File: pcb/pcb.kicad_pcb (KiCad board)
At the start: 2 copper layers, 266.7 x 76.2 mm, 116 parts, among them J1 USB_C_Receptacle_USB2.0, SW1 SW_Push, SW10 SW_Push, SW11 SW_Push, SW12 SW_Push, SW13 SW_Push, SW14 SW_Push, SW15 SW_Push, SW16 SW_Push, SW17 SW_Push, SW18 SW_Push, SW19 SW_Push, SW2 SW_Push, SW20 SW_Push, SW21 SW_Push, SW22 SW_Push, SW23 SW_Push, SW24 SW_Push, SW25 SW_Push, SW26 SW_Push, SW27 SW_Push, SW28 SW_Push, SW29 SW_Push, SW3 SW_Push, SW30 SW_Push, SW31 SW_Push, SW32 SW_Push, SW33 SW_Push, SW34 SW_Push, SW35 SW_Push, SW36 SW_Push, SW37 SW_Push, SW38 SW_Push, SW39 SW_Push, SW4 SW_Push, SW40 SW_Push, SW41 SW_Push, SW42 SW_Push, SW43 SW_Push, SW44 SW_Push, SW45 SW_Push, SW46 SW_Push, SW47 SW_Push, SW48 SW_Push, SW49 SW_Push, SW5 SW_Push, SW6 SW_Push, SW7 SW_Push, SW8 SW_Push, SW9 SW_Push, U1 ATmega32U4-AU, Y1 16MHz

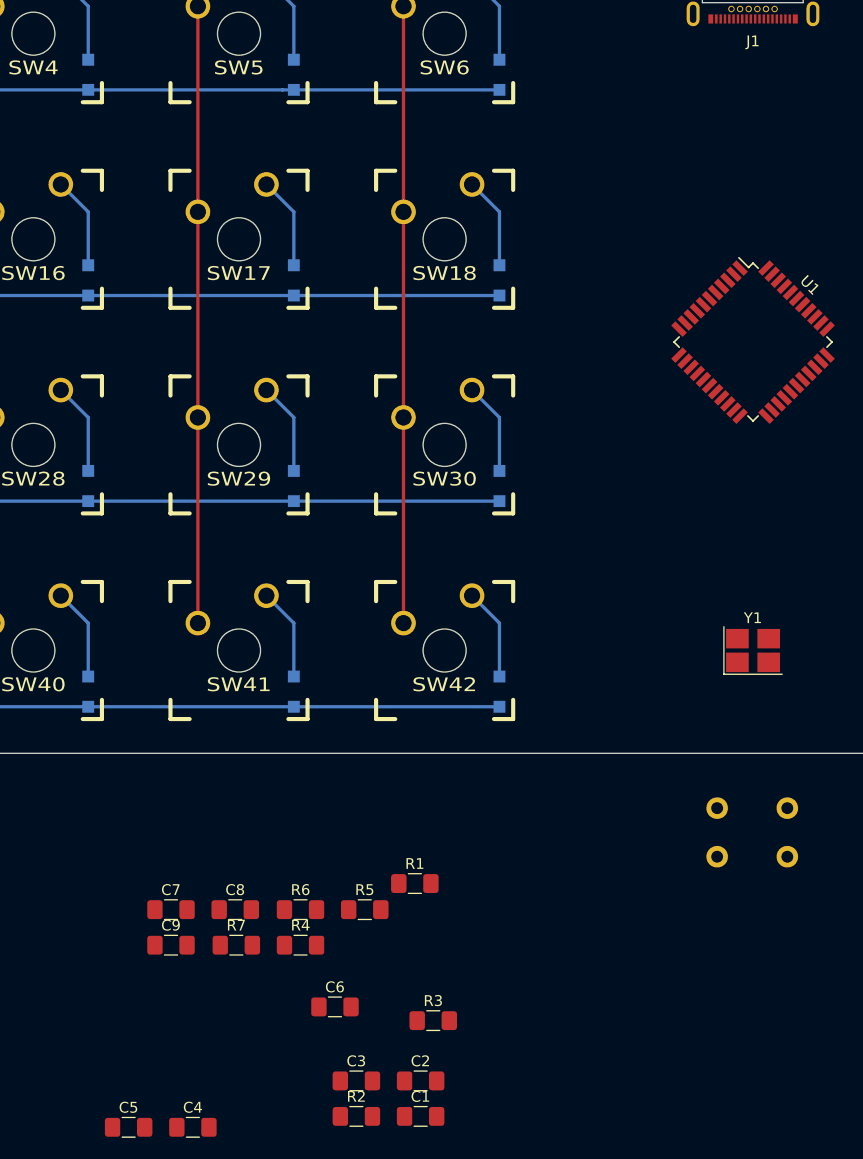
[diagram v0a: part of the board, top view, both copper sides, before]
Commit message: update USB-C pins
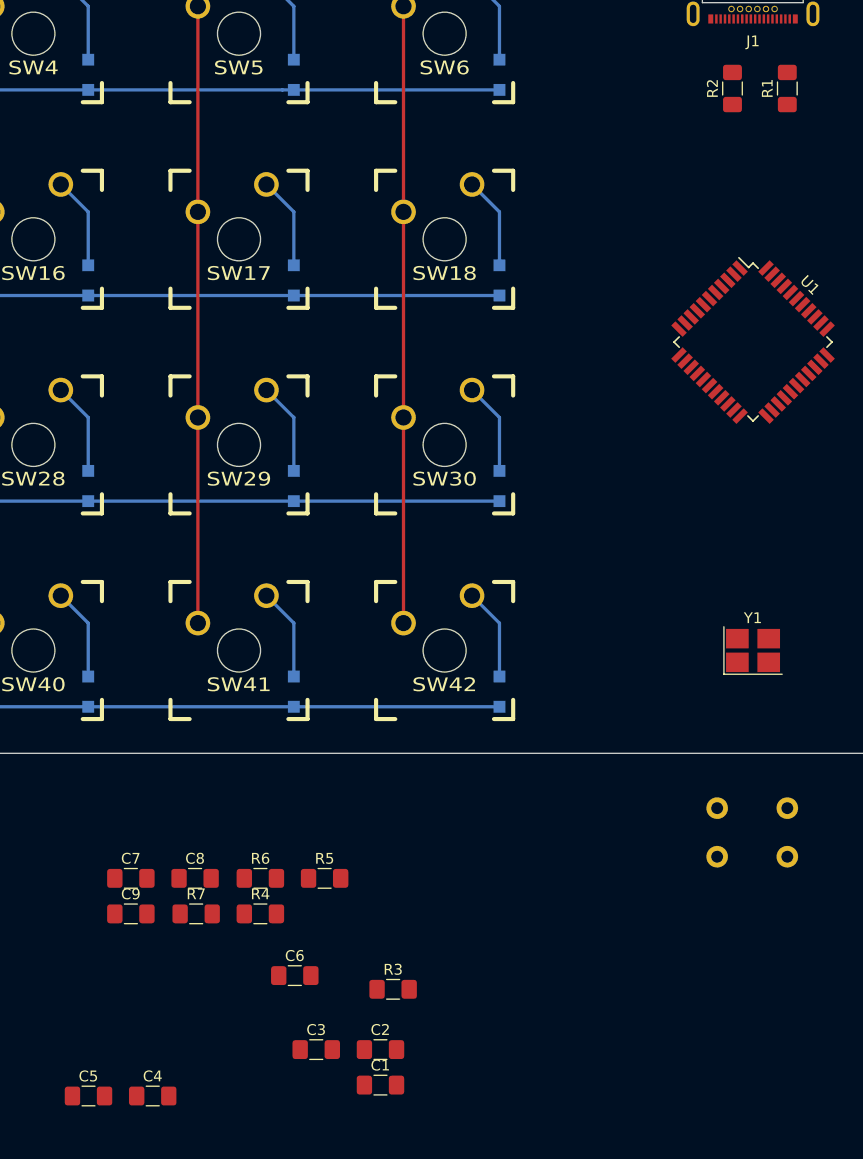
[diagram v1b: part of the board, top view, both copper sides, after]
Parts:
- moved R2 101.4 mm to (147.3, 43.2), turned to 90 degrees
- moved R1 81.3 mm to (152.4, 43.2), turned to 90 degrees
- moved C3 4.72 mm to (108.8, 132.2)
- moved R7 4.72 mm to (97.6, 119.7)
- moved C2 4.72 mm to (114.7, 132.2)
- moved C4 4.72 mm to (93.6, 136.5)
- moved C5 4.72 mm to (87.7, 136.5)
- moved C6 4.72 mm to (106.8, 125.4)
- moved C7 4.72 mm to (91.6, 116.4)
- moved C8 4.72 mm to (97.5, 116.4)
- moved R5 4.72 mm to (109.5, 116.4)
- moved R6 4.72 mm to (103.6, 116.4)
- moved C9 4.72 mm to (91.6, 119.7)
- moved R3 4.72 mm to (115.9, 126.6)
- moved R4 4.72 mm to (103.6, 119.7)
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
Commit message: add PCB & gerber
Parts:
- removed C3: 0.1u, Capacitor_SMD:C_1206_3216Metric_Pad1.42x1.75mm_HandSolder
- removed R6, R7: 22, Resistor_SMD:R_1206_3216Metric_Pad1.42x1.75mm_HandSolder
- removed SW49: SW_Push, Button_Switch_THT:SW_PUSH_6mm_H5mm
- added H1: MountingHole, MountingHole:MountingHole_3.5mm, F.Cu at (44.5, 47.6)
- added H2: MountingHole, MountingHole:MountingHole_3.5mm, F.Cu at (44.5, 85.7)
- added H3: MountingHole, MountingHole:MountingHole_3.5mm, F.Cu at (101.6, 47.6)
- added H4: MountingHole, MountingHole:MountingHole_3.5mm, F.Cu at (101.6, 85.7)
- added H5: MountingHole, MountingHole:MountingHole_3.5mm, F.Cu at (196.8, 47.6)
- added H6: MountingHole, MountingHole:MountingHole_3.5mm, F.Cu at (196.8, 85.7)
- added H7: MountingHole, MountingHole:MountingHole_3.5mm, F.Cu at (254.0, 47.6)
- added H8: MountingHole, MountingHole:MountingHole_3.5mm, F.Cu at (254.0, 85.7)
- added JP1: SolderJumper_2_Open, Jumper:SolderJumper-2_P1.3mm_Open_Pad1.0x1.5mm, F.Cu at (149.2, 103.5)
- J1: value USB_C_Receptacle_USB2.0 -> USB_C_Receptacle
- moved C5 101.8 mm to (145.4, 52.7), turned to 90 degrees
- moved C4 97.2 mm to (142.9, 52.7), turned to 90 degrees
- moved C9 89.2 mm to (150.5, 52.7), turned to 90 degrees
- moved R4 89.2 mm to (150.5, 43.8), turned to 90 degrees
- moved R3 88.8 mm to (148.0, 43.8), turned to 90 degrees
- moved C6 86.1 mm to (153.0, 52.7), turned to 90 degrees
- moved C8 63.9 mm to (150.5, 80.6), turned to 270 degrees
- moved C7 62.5 mm to (142.9, 80.6), turned to 270 degrees
- moved C1 59.4 mm to (153.0, 90.2), turned to 270 degrees
- moved C2 52.1 mm to (145.4, 90.2), turned to 270 degrees
- moved R5 50.6 mm to (145.4, 80.6), turned to 270 degrees
- moved SW12 9.53 mm to (263.5, 38.1)
- moved SW24 9.53 mm to (263.5, 57.1)
- moved SW36 9.53 mm to (263.5, 76.2)
- moved SW48 9.53 mm to (263.5, 95.2)
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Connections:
- J1 pad A4: VBUS -> VCC
- J1 pad A8: Net-(J1-PadA8) -> (no net)
- J1 pad A9: VBUS -> VCC
- J1 pad B4: VBUS -> VCC
- J1 pad B8: Net-(J1-PadB8) -> (no net)
- J1 pad B9: VBUS -> VCC
- U1 pad 1: Net-(U1-Pad1) -> (no net)
- U1 pad 12: C3 -> C5
- U1 pad 19: C5 -> C3
- U1 pad 20: C6 -> C2
- U1 pad 21: C7 -> C1
- U1 pad 22: C9 -> C0
- U1 pad 25: C8 -> C11
- U1 pad 27: C11 -> C9
- U1 pad 28: C0 -> C8
- U1 pad 29: C1 -> C7
- U1 pad 3: Net-(R7-Pad1) -> D-
- U1 pad 30: C2 -> C6
- U1 pad 31: Net-(U1-Pad31) -> (no net)
- U1 pad 32: Net-(U1-Pad32) -> (no net)
- U1 pad 36: Net-(U1-Pad36) -> (no net)
- U1 pad 37: Net-(U1-Pad37) -> (no net)
- U1 pad 38: Net-(U1-Pad38) -> (no net)
- U1 pad 39: Net-(U1-Pad39) -> (no net)
- U1 pad 4: Net-(R6-Pad1) -> D+
- U1 pad 40: Net-(U1-Pad40) -> (no net)
- U1 pad 41: Net-(U1-Pad41) -> (no net)
- U1 pad 42: Net-(C3-Pad1) -> (no net)
- U1 pad 7: VBUS -> VCC
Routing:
- net GND: track 0.00 -> 189.5 mm, vias 0 -> 10
- net C0: track 57.1 -> 185.3 mm, vias 0 -> 1
- net C11: track 57.1 -> 177.4 mm, vias 0 -> 1
- net VCC: track 0.00 -> 114.8 mm, vias 0 -> 4
- net C1: track 57.1 -> 164.6 mm, vias 0 -> 1
- net C10: track 57.1 -> 156.2 mm, vias 0 -> 1
- net C2: track 57.1 -> 143.1 mm, vias 0 -> 1
- net C9: track 57.1 -> 135.0 mm, vias 0 -> 1
- net R3: track 190.5 -> 267.0 mm, vias 0 -> 1
- net C3: track 57.1 -> 122.0 mm, vias 0 -> 1
- net R2: track 190.5 -> 252.3 mm, vias 0 -> 1
- net R0: track 190.5 -> 249.0 mm, vias 0 -> 3
- net C8: track 57.1 -> 113.8 mm, vias 0 -> 1
- net R1: track 190.5 -> 235.7 mm, vias 0 -> 1
- net C4: track 57.1 -> 100.8 mm, vias 0 -> 1
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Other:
- board size 266.7 x 76.2 mm -> 247.7 x 76.2 mm
- board text added: "Designed by Kakudo. ver.0"
